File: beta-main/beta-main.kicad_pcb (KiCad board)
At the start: 4 copper layers, 76 x 121 mm, 93 parts, among them J1 Conn_01x02_Pin, J10 Conn_01x03_Pin, J11 Conn_01x03_Pin, J12 Conn_01x03_Pin, J13 Conn_01x03_Pin, J14 Conn_01x04_Pin, J15 Conn_01x04_Pin, J16 Conn_01x04_Pin, J17 Conn_01x04_Pin, J18 XT60, J19 Conn_01x02_Pin, J2 Conn_01x08_Pin, J20 Conn_01x02_Pin, J21 Conn_01x02_Pin, J22 Conn_01x06_Pin, J23 Conn_01x06_Pin, J24 Conn_01x02_Pin, J25 Conn_01x02_Pin, J26 Conn_01x04_Pin, J3 Conn_01x08_Pin, J5 FFC, J8 FFC, Q1 MMBT3906, Q2 IRLML6246TRP, U1 MAX98357A, U2 74LVC1G126, U3 BNO086, U4 74LVC1G126, U5 AP3441SHE-7B, U6 TPS56624x, U7 AP2553W6

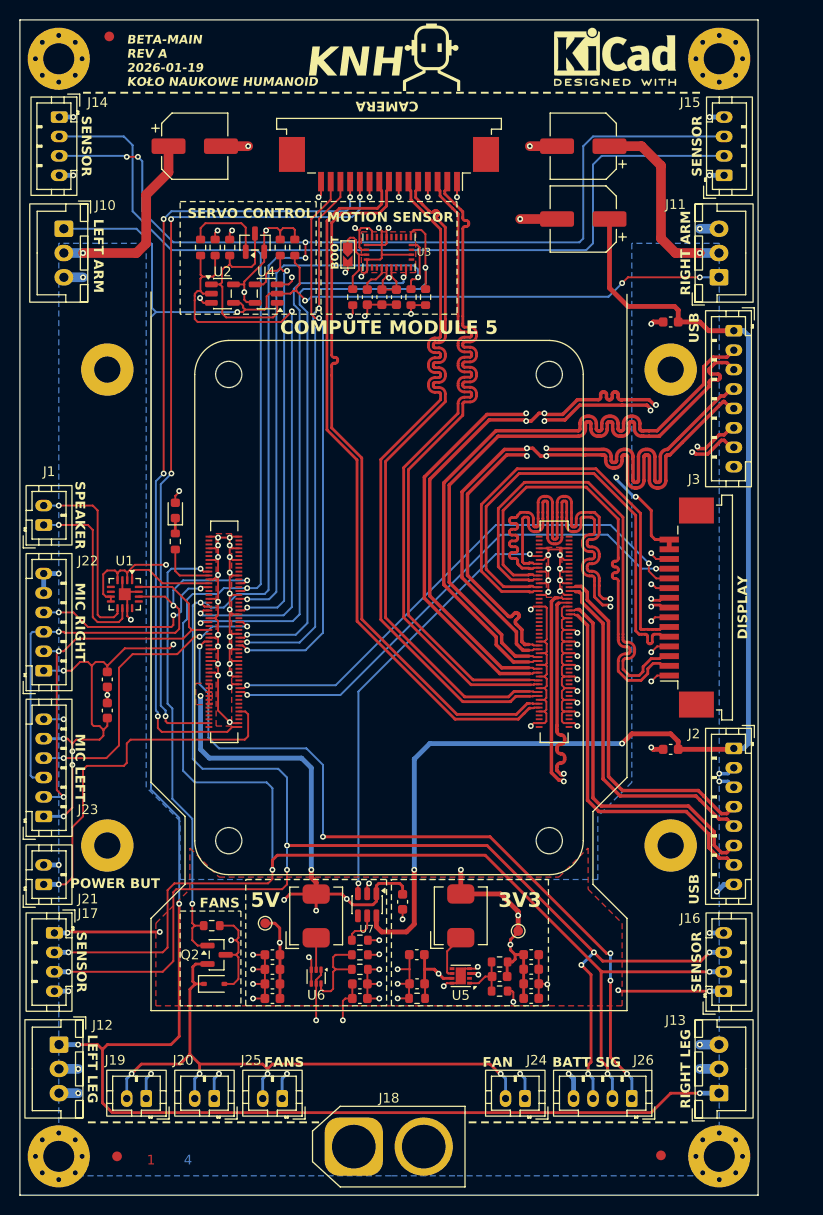
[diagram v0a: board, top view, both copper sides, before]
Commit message: add schematic's plot
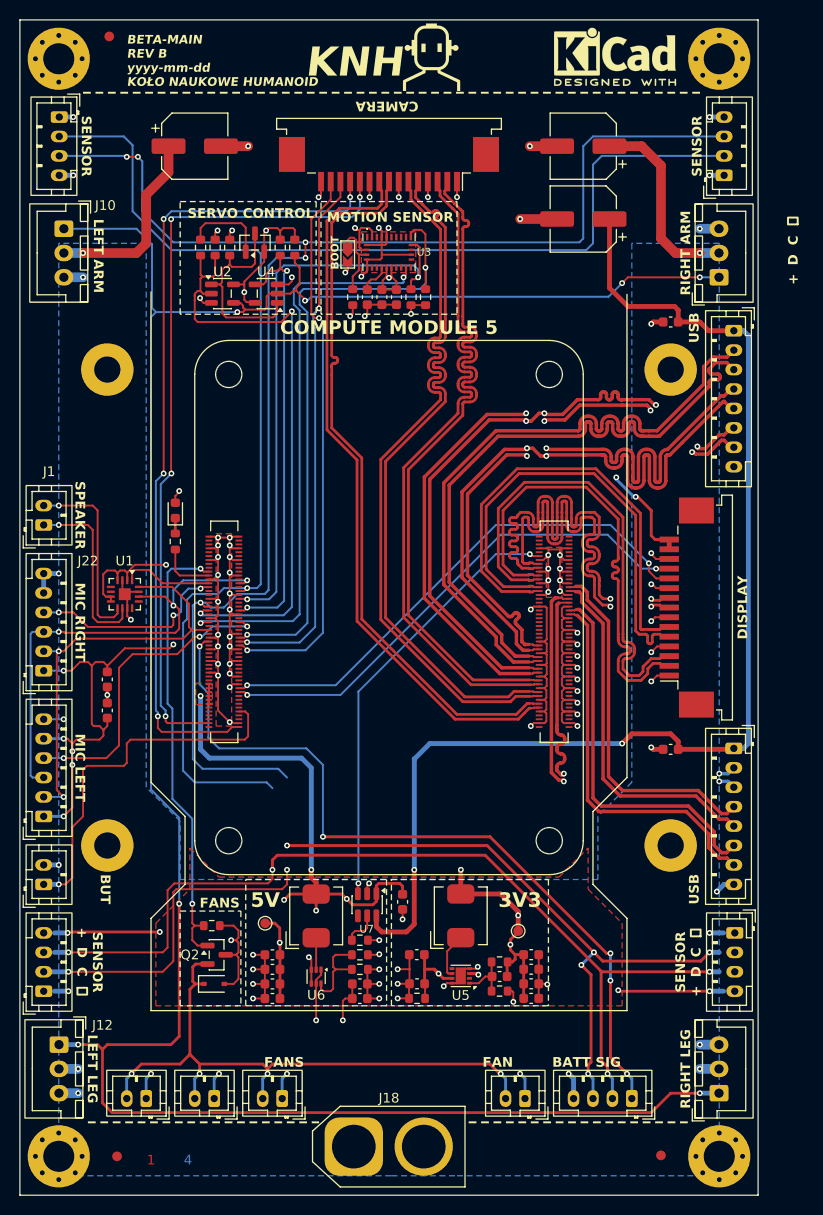
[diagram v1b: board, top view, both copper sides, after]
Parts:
- moved J16 6.11 mm to (135.6, 133.5), turned to -90 degrees
- moved J17 6.10 mm to (64.5, 139.5), turned to 90 degrees
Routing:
- net /Peripherals/SENSOR_SCL: track 270.0 -> 226.7 mm, vias 12 -> 10
- net /Peripherals/SENSOR_SDA: track 261.9 -> 287.5 mm, vias 5 -> 7
- net GND: track 265.5 -> 275.0 mm, vias 95 -> 96
- net +3V3: track 148.8 -> 139.4 mm, vias 28 -> 27
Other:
- board text added: "+"
- board text added: "BETA-MAIN REV B yyyy-mm-dd KOŁO NAUKOWE HUMANOID"
- board text added: "BUT"
- board text added: "C"
- board text added: "D"
- board text added: "⏚"
- board text removed: "BETA-MAIN REV A 2026-01-19 KOŁO NAUKOWE HUMANOID"
- board text removed: "POWER BUT"
